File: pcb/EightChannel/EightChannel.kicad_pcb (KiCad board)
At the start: 2 copper layers, 57.1 x 83.8 mm, 41 parts, among them J101 Barrel_Jack_Switch, J102 UDP, J103 Conn_01x07_Female, J104 Conn_01x07_Female, J201 Strip 0, J202 Strip 2, J203 Strip 4, J204 Strip 6, J205 Strip 1, J206 Strip 3, J207 Strip 5, J208 Strip 7, M101 NODEMCU_ESP8266, U101 ATtiny1614-SS, U102 74LS595

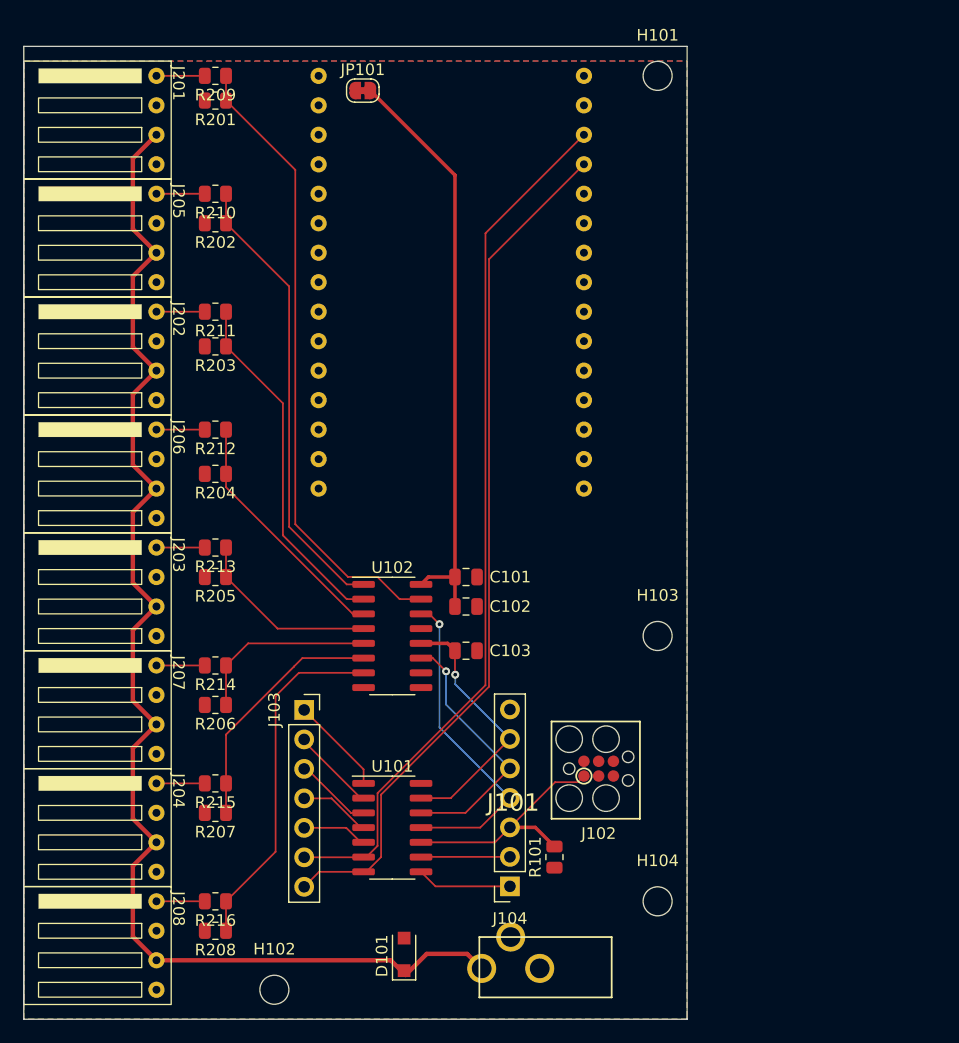
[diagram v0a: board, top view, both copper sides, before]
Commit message: Finished 8Channel and submitted to Fab
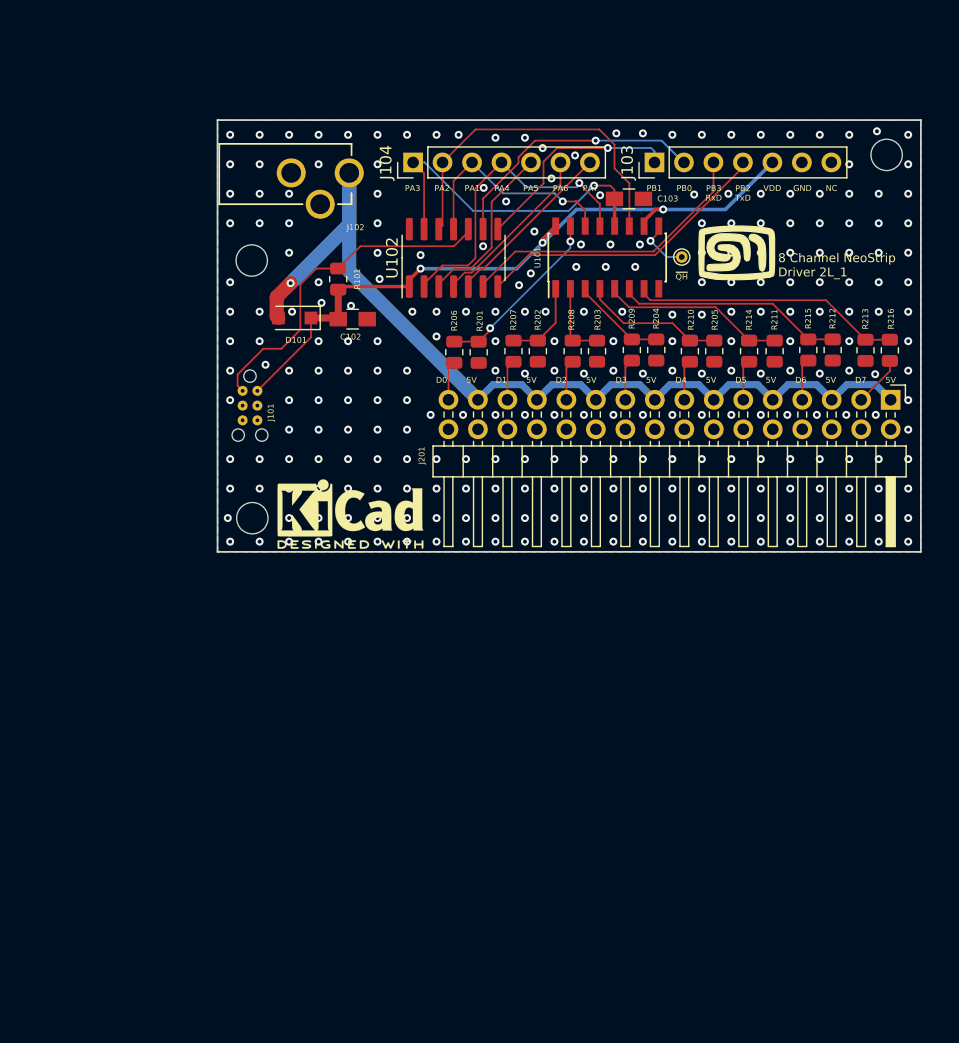
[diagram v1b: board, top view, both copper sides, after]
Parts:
- removed C101: 1μF 16V, Capacitor_SMD:C_0805_2012Metric
- removed H104: MountingHole, MountingHole:MountingHole_2.5mm
- removed J202: Strip 2, advent_sternla:CONN_ANGLED_4_2.54
- removed J203: Strip 4, advent_sternla:CONN_ANGLED_4_2.54
- removed J204: Strip 6, advent_sternla:CONN_ANGLED_4_2.54
- removed J205: Strip 1, advent_sternla:CONN_ANGLED_4_2.54
- removed J206: Strip 3, advent_sternla:CONN_ANGLED_4_2.54
- removed J207: Strip 5, advent_sternla:CONN_ANGLED_4_2.54
- removed J208: Strip 7, advent_sternla:CONN_ANGLED_4_2.54
- removed JP101: Ext, Jumper:SolderJumper-2_P1.3mm_Bridged_RoundedPad1.0x1.5mm
- removed M101: NODEMCU_ESP8266, advent_sternla:NODEMCU_ESP8266
- added Lg101: logo, mech:MyBasic_rounded_50_1, F.Cu at (155.4, 54.6)
- added Lg102: logo, Symbol:KiCad-Logo2_5mm_SilkScreen, F.Cu at (122.1, 77.1)
- added Lg103: logo, advent_sternla:QR_AdventSternla_FS, B.Cu at (162.6, 57.1)
- added TP101: TestPoint, TestPoint:TestPoint_THTPad_D1.0mm_Drill0.5mm, F.Cu at (150.7, 55.0)
- C102: value 100nF -> 1μF 16V; footprint Capacitor_SMD:C_0805_2012Metric -> Capacitors_SMD:C_0805_HandSoldering
- C103: footprint Capacitor_SMD:C_0805_2012Metric -> Capacitors_SMD:C_0805_HandSoldering
- D101: footprint Diode_SMD:D_SOD-123F -> Diodes_SMD:D_SOD-123F
- H101, H102, H103: footprint MountingHole:MountingHole_2.5mm -> MountingHole:MountingHole_2.7mm_M2.5
- J101: value Barrel_Jack_Switch -> UPDI; footprint advent_sternla:CONN_PWR_JACK_1_3X3_5MM_SOLDER -> advent_sternla:PRG_TC2030-IDC-NL
- J102: value UDP -> 5V In; footprint advent_sternla:TC2030-IDC-FP_ISP_Connector -> advent_sternla:CONN_PWR_JACK_1_3X3_5MM_SOLDER
- J103: value Conn_01x07_Female -> GPIO1; footprint Connector_PinSocket_2.54mm:PinSocket_1x07_P2.54mm_Vertical -> Connector_PinHeader_2.54mm:PinHeader_1x07_P2.54mm_Vertical
- J104: value Conn_01x07_Female -> GPIO2; footprint Connector_PinSocket_2.54mm:PinSocket_1x07_P2.54mm_Vertical -> Connector_PinHeader_2.54mm:PinHeader_1x07_P2.54mm_Vertical
- J201: value Strip 0 -> NEO STRIPS; footprint advent_sternla:CONN_ANGLED_4_2.54 -> Connector_PinHeader_2.54mm:PinHeader_2x16_P2.54mm_Horizontal
- R201, R202, R203, R204, R205: value 10k -> 10kΩ
- R206, R207, R208: value 10k -> 470Ω
- R209, R210, R214, R215, R216: value 470 -> 470Ω
- R211, R212, R213: value 470 -> 10kΩ
- U101: value ATtiny1614-SS -> 74LS595; footprint Package_SO:SOIC-14_3.9x8.7mm_P1.27mm -> Housings_SOIC:SOIC-16_3.9x9.9mm_Pitch1.27mm
- U102: value 74LS595 -> ATTINY1614; footprint Package_SO:SOIC-16_3.9x9.9mm_P1.27mm -> Package_SO:SOIC-14_3.9x8.7mm_P1.27mm
- moved R216 75.0 mm to (168.6, 63.0), turned to -90 degrees
- moved J201 69.1 mm to (168.7, 67.3)
- moved R215 63.3 mm to (161.6, 63.0), turned to -90 degrees
- moved J104 62.9 mm to (127.5, 46.8), turned to 90 degrees
- moved H102 62.9 mm to (113.6, 55.3)
- moved R208 58.7 mm to (141.3, 63.1), turned to -90 degrees
- moved R213 58.5 mm to (166.5, 63.0), turned to 90 degrees
- moved J102 56.7 mm to (119.5, 47.7)
- moved J103 56.0 mm to (148.3, 46.8), turned to 90 degrees
- moved D101 55.6 mm to (117.3, 60.2), turned to 180 degrees
- moved J101 54.9 mm to (112.8, 66.5), turned to -90 degrees
- moved R212 53.6 mm to (163.7, 63.0), turned to 90 degrees
- moved R214 53.4 mm to (156.5, 63.1), turned to -90 degrees
- moved R101 53.2 mm to (121.1, 56.9), turned to -90 degrees
- moved U101 52.5 mm to (144.2, 55.0), turned to 90 degrees
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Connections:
- C103 pad 1: /PA3_LATCH -> /LATCH_PIN
- D101 pad 1: /5V_OUT -> /VDD
- D101 pad 2: /VDD -> /5V_OUT
- J101 pad 1: /5V_OUT -> /PDI_DATA
- J101 pad 2: GND -> /VDD
- J102 pad 1: /PA0_PDI -> /5V_OUT
- J102 pad 2: /VDD -> GND
- J103 pad 1: /VDD -> /PB1
- J103 pad 2: /PA4_~{ENABLE} -> /PB0
- J103 pad 3: /PA5 -> /PB3_RxD
- J103 pad 4: /PA6 -> /PB2_TxD
- J103 pad 5: /PA7 -> /VDD
- J103 pad 6: /PB3_RxD -> GND
- J103 pad 7: /PB2_TxD -> unconnected-(J103-Pad7)
- J104 pad 1: /PB1 -> /LATCH_PIN
- J104 pad 2: /PB0 -> /CLK_PIN
- J104 pad 3: /PA0_PDI -> /DATA_PIN
- J104 pad 4: /PA1_DATA -> /~{ENABLE}
- J104 pad 5: /PA2_CLK -> /PA5
- J104 pad 6: /PA3_LATCH -> /PA6
- J104 pad 7: GND -> /PA7
- J201 pad 1: /Channels/NP_DATA_0 -> /5V_OUT
- J201 pad 3: /5V_OUT -> /Channels/NP_DATA_7
- R101 pad 1: /VDD -> /PDI_DATA
- R101 pad 2: /PA0_PDI -> /VDD
- R201 pad 1: /CHANNEL_0 -> GND
- R201 pad 2: GND -> /CHANNEL_0
- R202 pad 1: /CHANNEL_1 -> GND
- R202 pad 2: GND -> /CHANNEL_1
- R203 pad 1: /CHANNEL_2 -> GND
- R203 pad 2: GND -> /CHANNEL_2
- R204 pad 1: /CHANNEL_3 -> GND
- R204 pad 2: GND -> /CHANNEL_3
- R205 pad 1: /CHANNEL_4 -> GND
- R205 pad 2: GND -> /CHANNEL_4
- R206 pad 1: /CHANNEL_5 -> /CHANNEL_0
- R206 pad 2: GND -> /Channels/NP_DATA_0
- R207 pad 1: /CHANNEL_6 -> /CHANNEL_1
- R207 pad 2: GND -> /Channels/NP_DATA_1
- R208 pad 1: /CHANNEL_7 -> /CHANNEL_2
- R208 pad 2: GND -> /Channels/NP_DATA_2
- R209 pad 1: /CHANNEL_0 -> /CHANNEL_3
- R209 pad 2: /Channels/NP_DATA_0 -> /Channels/NP_DATA_3
- R210 pad 1: /CHANNEL_1 -> /CHANNEL_4
- R210 pad 2: /Channels/NP_DATA_1 -> /Channels/NP_DATA_4
- R211 pad 1: /CHANNEL_2 -> GND
- R211 pad 2: /Channels/NP_DATA_2 -> /CHANNEL_5
- R212 pad 1: /CHANNEL_3 -> GND
- R212 pad 2: /Channels/NP_DATA_3 -> /CHANNEL_6
- R213 pad 1: /CHANNEL_4 -> GND
- R213 pad 2: /Channels/NP_DATA_4 -> /CHANNEL_7
- U101 pad 1: /VDD -> /CHANNEL_1
- U101 pad 10: /PA0_PDI -> /VDD
- U101 pad 11: /PA1_DATA -> /CLK_PIN
- U101 pad 12: /PA2_CLK -> /LATCH_PIN
- U101 pad 13: /PA3_LATCH -> /~{ENABLE}
- U101 pad 14: GND -> /DATA_PIN
- U101 pad 2: /PA4_~{ENABLE} -> /CHANNEL_2
- U101 pad 3: /PA5 -> /CHANNEL_3
- U101 pad 4: /PA6 -> /CHANNEL_4
- U101 pad 5: /PA7 -> /CHANNEL_5
- U101 pad 6: /PB3_RxD -> /CHANNEL_6
- U101 pad 7: /PB2_TxD -> /CHANNEL_7
- U101 pad 8: /PB1 -> GND
- U101 pad 9: /PB0 -> Net-(TP101-Pad1)
- U102 pad 1: /CHANNEL_1 -> /VDD
- U102 pad 10: /VDD -> /PDI_DATA
- U102 pad 11: /PA2_CLK -> /DATA_PIN
- U102 pad 12: /PA3_LATCH -> /CLK_PIN
- U102 pad 13: /PA4_~{ENABLE} -> /LATCH_PIN
- U102 pad 14: /PA1_DATA -> GND
- U102 pad 2: /CHANNEL_2 -> /~{ENABLE}
- U102 pad 3: /CHANNEL_3 -> /PA5
- U102 pad 4: /CHANNEL_4 -> /PA6
- U102 pad 5: /CHANNEL_5 -> /PA7
- U102 pad 6: /CHANNEL_6 -> /PB3_RxD
- U102 pad 7: /CHANNEL_7 -> /PB2_TxD
- U102 pad 8: GND -> /PB1
- U102 pad 9: unconnected-(U102-Pad9) -> /PB0
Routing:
- net /PB3_RxD: track 75.4 -> 25.9 mm
- net /PB2_TxD: track 74.6 -> 25.8 mm
- net /CHANNEL_0: track 54.6 -> 15.3 mm, vias 0 -> 2
- net /CHANNEL_1: track 39.4 -> 7.19 mm
- net /5V_OUT: track 112.7 -> 82.4 mm, vias 0 -> 1
- net /CLK_PIN: track 0.00 -> 30.0 mm
- net /LATCH_PIN: track 0.00 -> 29.4 mm, vias 0 -> 1
- net /PDI_DATA: track 0.00 -> 29.1 mm
- net /PA1_DATA: track 28.2 -> 0.00 mm, vias 1 -> 0
- net /~{ENABLE}: track 0.00 -> 27.0 mm, vias 0 -> 1
- net /CHANNEL_2: track 30.5 -> 6.64 mm
- net /PA3_LATCH: track 22.5 -> 0.00 mm, vias 1 -> 0
- net /PA2_CLK: track 22.5 -> 0.00 mm, vias 1 -> 0
- net /PA0_PDI: track 20.9 -> 0.00 mm
- net /DATA_PIN: track 0.00 -> 19.2 mm, vias 0 -> 1
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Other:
- board size 57.1 x 83.8 mm -> 60.6 x 37.2 mm
- board text added: "5V"
- board text added: "8 Channel NeoStrip Driver 2L_1"
- board text added: "D0"
- board text added: "D1"
- board text added: "D2"
- board text added: "D3"
- board text added: "D4"
- board text added: "D5"
- board text added: "D6"
- board text added: "D7"
- board text added: "GND"
- board text added: "NC"
- board text added: "PA1"
- board text added: "PA2"
- board text added: "PA3"
- board text added: "PA4"
- board text added: "PA5"
- board text added: "PA6"
- board text added: "PA7"
- board text added: "PB0"
- board text added: "PB1"
- board text added: "PB2 TxD"
- board text added: "PB3 RxD"
- board text added: "VDD"
- board text added: "~{QH}"

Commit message: Update and synch of the eight channel design
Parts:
- R201, R202, R203, R204, R205, R211, R212, R213: value 10kΩ -> 1kΩ
- R206, R207, R208, R209, R210, R214, R215, R216: value 470Ω -> 0Ω
